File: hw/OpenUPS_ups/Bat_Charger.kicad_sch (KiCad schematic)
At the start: 63 parts, among them Q406 AON7423, Q601 2N7002, Q701 AON7534, U402 BD99950, U403 MCP6001R, U404 DZDH0401DW, U405 INA180A1, U801 NCP431

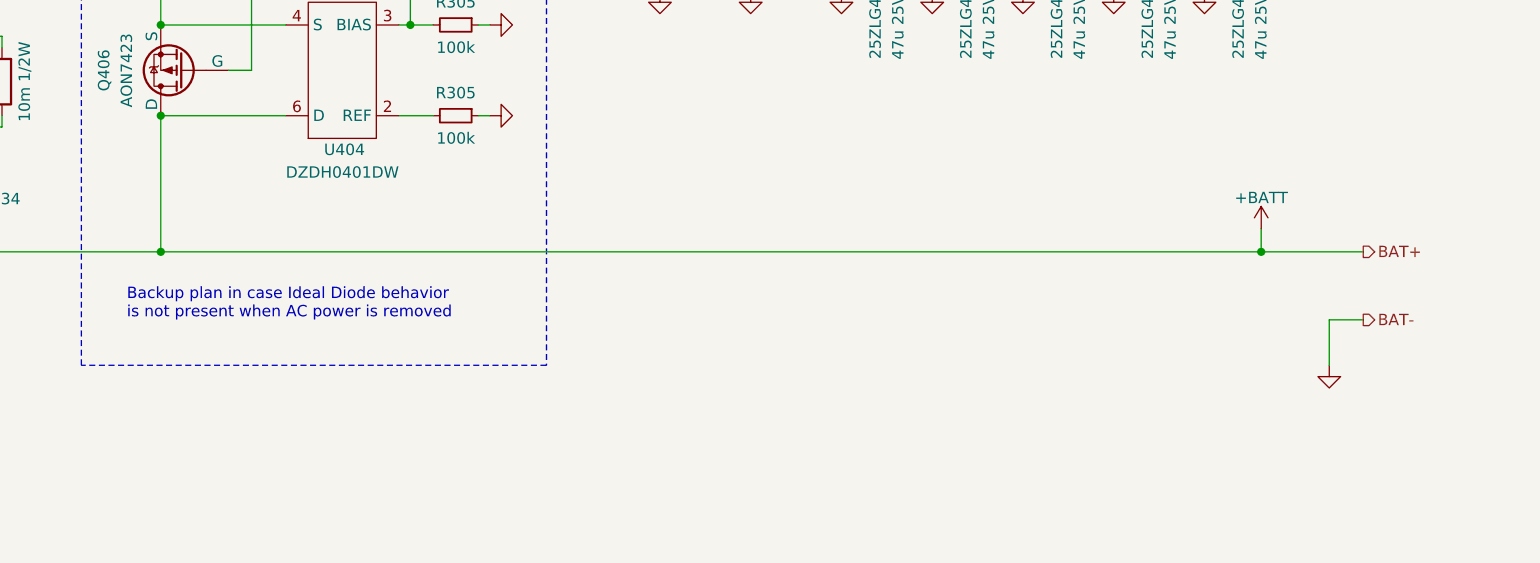
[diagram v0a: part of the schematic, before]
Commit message: BMS implementation complete (on schematic)
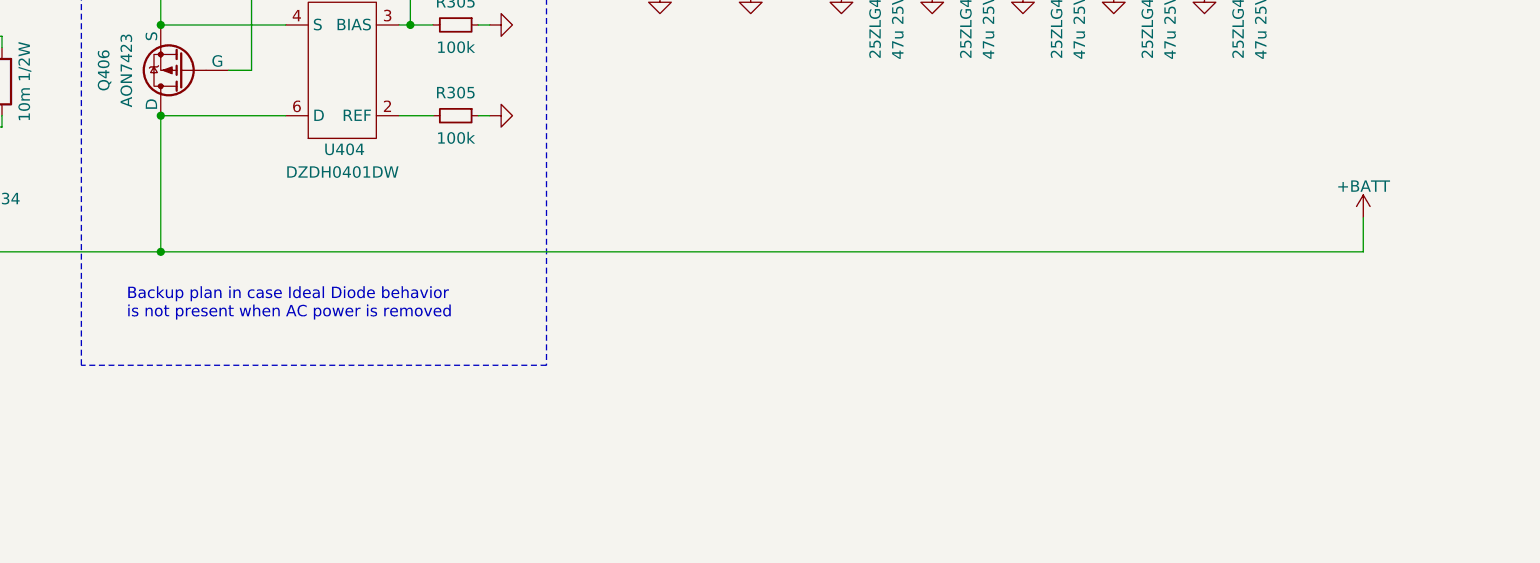
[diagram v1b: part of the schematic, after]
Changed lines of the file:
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@@
   (junction (at 240.03 217.17) (diameter 0) (color 0 0 0 0)
   )
-  (junction (at 368.3 102.87) (diameter 0) (color 0 0 0 0)
-  )
   (junction (at 218.44 60.96) (diameter 0) (color 0 0 0 0)
   )
@@
     (stroke (width 0) (type default))
   )
-  (wire (pts (xy 375.92 110.49) (xy 379.73 110.49))
-    (stroke (width 0) (type default))
-  )
   (wire (pts (xy 273.05 77.47) (xy 275.59 77.47))
     (stroke (width 0) (type default))
@@
     (stroke (width 0) (type default))
   )
-  (wire (pts (xy 375.92 110.49) (xy 375.92 115.57))
-    (stroke (width 0) (type default))
-  )
   (wire (pts (xy 209.55 102.87) (xy 209.55 101.6))
     (stroke (width 0) (type default))
@@
     (stroke (width 0) (type default))
   )
-  (wire (pts (xy 368.3 100.33) (xy 368.3 102.87))
+  (wire (pts (xy 379.73 99.06) (xy 379.73 102.87))
     (stroke (width 0) (type default))
   )
@@
     (stroke (width 0) (type default))
   )
-  (wire (pts (xy 245.11 102.87) (xy 368.3 102.87))
+  (wire (pts (xy 245.11 102.87) (xy 379.73 102.87))
     (stroke (width 0) (type default))
   )
@@
     (stroke (width 0) (type default))
   )
-  (wire (pts (xy 368.3 102.87) (xy 379.73 102.87))
-    (stroke (width 0) (type default))
-  )
   (wire (pts (xy 252.73 82.55) (xy 255.27 82.55))
     (stroke (width 0) (type default))
@@
     (effects (font (size 1.27 1.27)) (justify right))
   )
-  (hierarchical_label "BAT-" (shape output) (at 379.73 110.49 0) (fields_autoplaced)
-    (effects (font (size 1.27 1.27)) (justify left))
-  )
   (hierarchical_label "BAT_I" (shape output) (at 318.77 214.63 180) (fields_autoplaced)
     (effects (font (size 1.27 1.27)) (justify right))
@@
     (effects (font (size 1.27 1.27)) (justify right))
   )
-  (hierarchical_label "BAT+" (shape output) (at 379.73 102.87 0) (fields_autoplaced)
-    (effects (font (size 1.27 1.27)) (justify left))
-  )
   (hierarchical_label "SCL" (shape input) (at 80.01 105.41 180) (fields_autoplaced)
     (effects (font (size 1.27 1.27)) (justify right))
@@
   (symbol (lib_id "power:+3.3VA") (at 255.27 201.93 0) (unit 1)
     (in_bom yes) (on_board yes) (dnp no) (fields_autoplaced)
-    (property "Reference" "#PWR0102" (at 255.27 205.74 0)
+    (property "Reference" "#PWR?" (at 255.27 205.74 0)
       (effects (font (size 1.27 1.27)) hide)
     )
@@
       (project "OpenUPS_ups"
         (path "/f77faec3-eac4-47f3-a2de-ec4a039f4502"
-          (reference "#PWR0102") (unit 1)
+          (reference "#PWR?") (unit 1)
         )
         (path "/f77faec3-eac4-47f3-a2de-ec4a039f4502/0bd99307-a15c-41e8-997b-077d576f806c"
@@
     )
   )
-  (symbol (lib_id "power:GND") (at 375.92 115.57 0) (unit 1)
-    (in_bom yes) (on_board yes) (dnp no)
-    (property "Reference" "#PWR0306" (at 375.92 121.92 0)
-      (effects (font (size 1.27 1.27)) hide)
-    )
-    (property "Value" "GND" (at 375.92 119.38 0)
-      (effects (font (size 1.27 1.27)) hide)
-    )
-    (property "Footprint" "" (at 375.92 115.57 0)
-      (effects (font (size 1.27 1.27)))
-    )
-    (property "Datasheet" "" (at 375.92 115.57 0)
-      (effects (font (size 1.27 1.27)))
-    )
-    (pin "1")
-    (instances
-      (project "OpenUPS_ups"
-        (path "/f77faec3-eac4-47f3-a2de-ec4a039f4502/c1f639ea-b62e-4979-b175-523e44c4a4ee"
-          (reference "#PWR0306") (unit 1)
-        )
-        (path "/f77faec3-eac4-47f3-a2de-ec4a039f4502/0bd99307-a15c-41e8-997b-077d576f806c"
-          (reference "#PWR0440") (unit 1)
-        )
-      )
-    )
-  )
   (symbol (lib_id "Device:C_Small") (at 209.55 99.06 0) (mirror y) (unit 1)
     (in_bom yes) (on_board yes) (dnp no)
@@
   (symbol (lib_id "power:+3.3VA") (at 96.52 90.17 0) (unit 1)
     (in_bom yes) (on_board yes) (dnp no) (fields_autoplaced)
-    (property "Reference" "#PWR0102" (at 96.52 93.98 0)
+    (property "Reference" "#PWR?" (at 96.52 93.98 0)
       (effects (font (size 1.27 1.27)) hide)
     )
@@
       (project "OpenUPS_ups"
         (path "/f77faec3-eac4-47f3-a2de-ec4a039f4502"
-          (reference "#PWR0102") (unit 1)
+          (reference "#PWR?") (unit 1)
         )
         (path "/f77faec3-eac4-47f3-a2de-ec4a039f4502/0bd99307-a15c-41e8-997b-077d576f806c"
@@
   (symbol (lib_id "power:+3.3VA") (at 356.87 201.93 0) (unit 1)
     (in_bom yes) (on_board yes) (dnp no) (fields_autoplaced)
-    (property "Reference" "#PWR0102" (at 356.87 205.74 0)
+    (property "Reference" "#PWR?" (at 356.87 205.74 0)
       (effects (font (size 1.27 1.27)) hide)
     )
@@
       (project "OpenUPS_ups"
         (path "/f77faec3-eac4-47f3-a2de-ec4a039f4502"
-          (reference "#PWR0102") (unit 1)
+          (reference "#PWR?") (unit 1)
         )
         (path "/f77faec3-eac4-47f3-a2de-ec4a039f4502/0bd99307-a15c-41e8-997b-077d576f806c"
@@
     )
   )
-  (symbol (lib_id "power:+BATT") (at 368.3 100.33 0) (unit 1)
+  (symbol (lib_id "power:+BATT") (at 379.73 99.06 0) (unit 1)
     (in_bom yes) (on_board yes) (dnp no) (fields_autoplaced)
-    (property "Reference" "#PWR0439" (at 368.3 104.14 0)
+    (property "Reference" "#PWR0439" (at 379.73 102.87 0)
       (effects (font (size 1.27 1.27)) hide)
     )
-    (property "Value" "+BATT" (at 368.3 96.8281 0)
+    (property "Value" "+BATT" (at 379.73 95.5581 0)
       (effects (font (size 1.27 1.27)))
     )
-    (property "Footprint" "" (at 368.3 100.33 0)
+    (property "Footprint" "" (at 379.73 99.06 0)
       (effects (font (size 1.27 1.27)) hide)
     )
-    (property "Datasheet" "" (at 368.3 100.33 0)
+    (property "Datasheet" "" (at 379.73 99.06 0)
       (effects (font (size 1.27 1.27)) hide)
     )
@@
   (symbol (lib_id "power:+3.3VA") (at 87.63 90.17 0) (unit 1)
     (in_bom yes) (on_board yes) (dnp no) (fields_autoplaced)
-    (property "Reference" "#PWR0102" (at 87.63 93.98 0)
+    (property "Reference" "#PWR?" (at 87.63 93.98 0)
       (effects (font (size 1.27 1.27)) hide)
     )
@@
       (project "OpenUPS_ups"
         (path "/f77faec3-eac4-47f3-a2de-ec4a039f4502"
-          (reference "#PWR0102") (unit 1)
+          (reference "#PWR?") (unit 1)
         )
         (path "/f77faec3-eac4-47f3-a2de-ec4a039f4502/0bd99307-a15c-41e8-997b-077d576f806c"
